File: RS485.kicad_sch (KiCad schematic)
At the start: 18 parts, among them CN4 WJ15EDGRC-3.81-2P, Q3 CJ3134K, U11 CA-IS3721HS, U12 π131U30, U13 SIT3485ESA, U14 ISO3082DWR

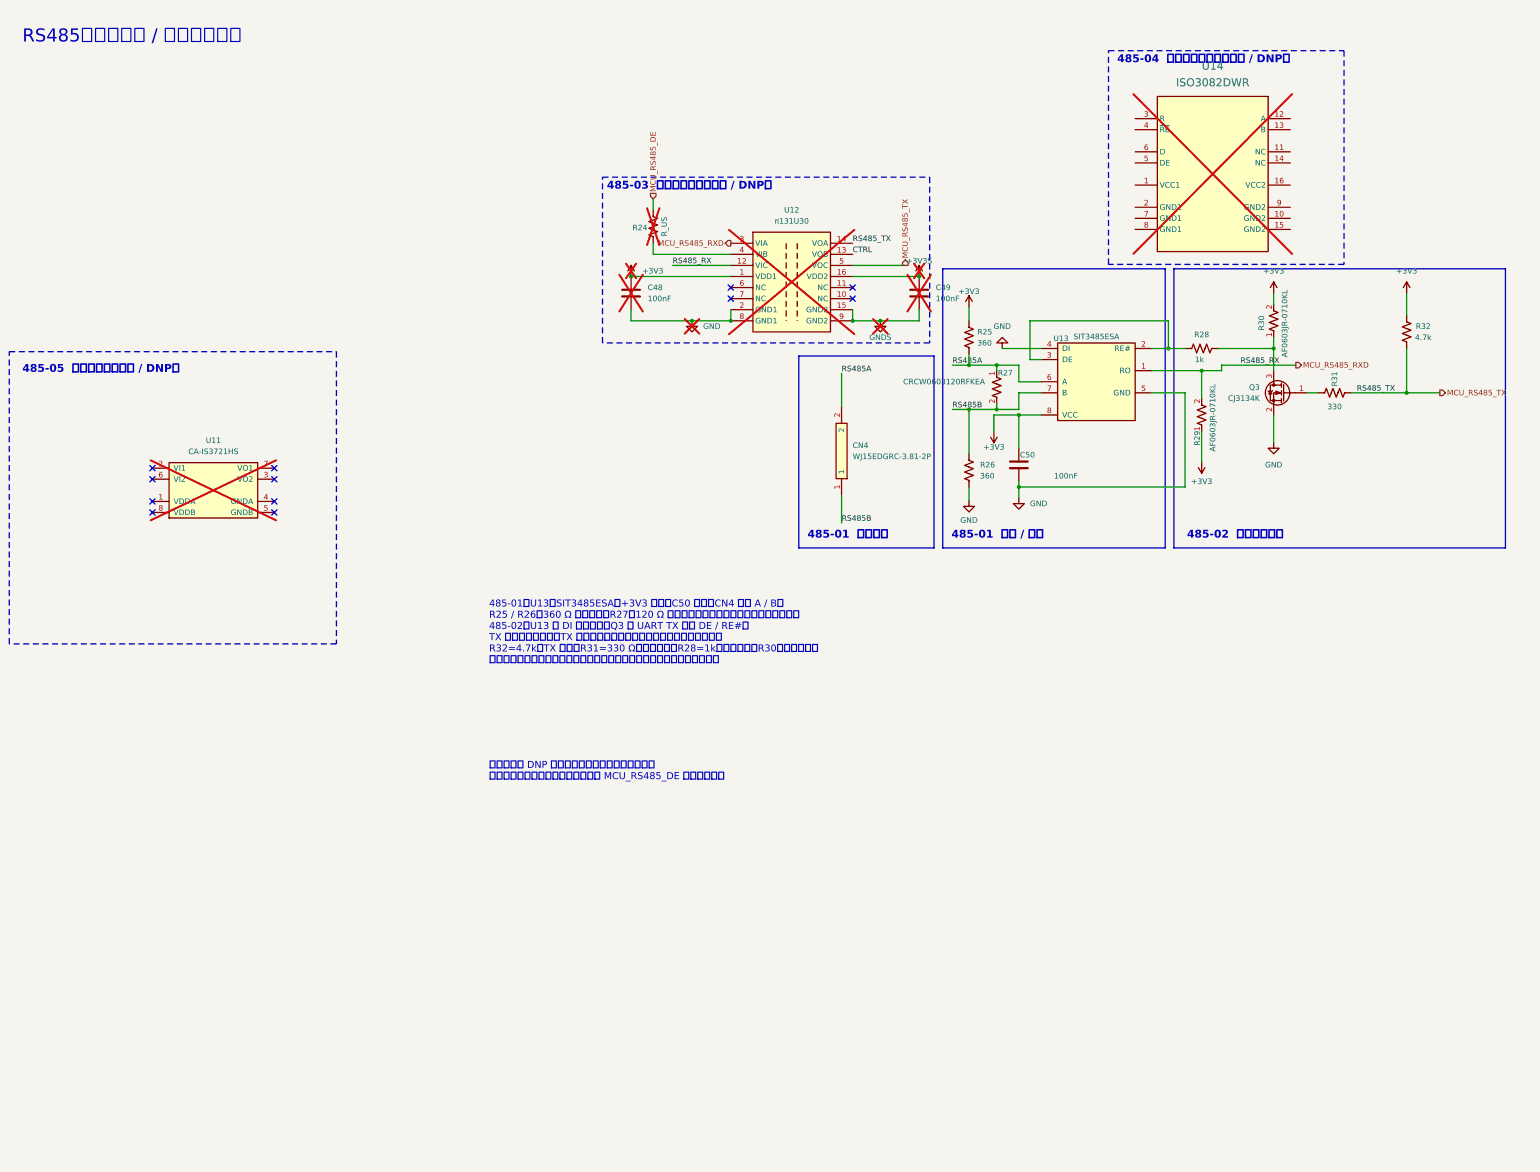
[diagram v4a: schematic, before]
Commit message: 更新V2.0电路设计及0.5oz内层制造交付资料
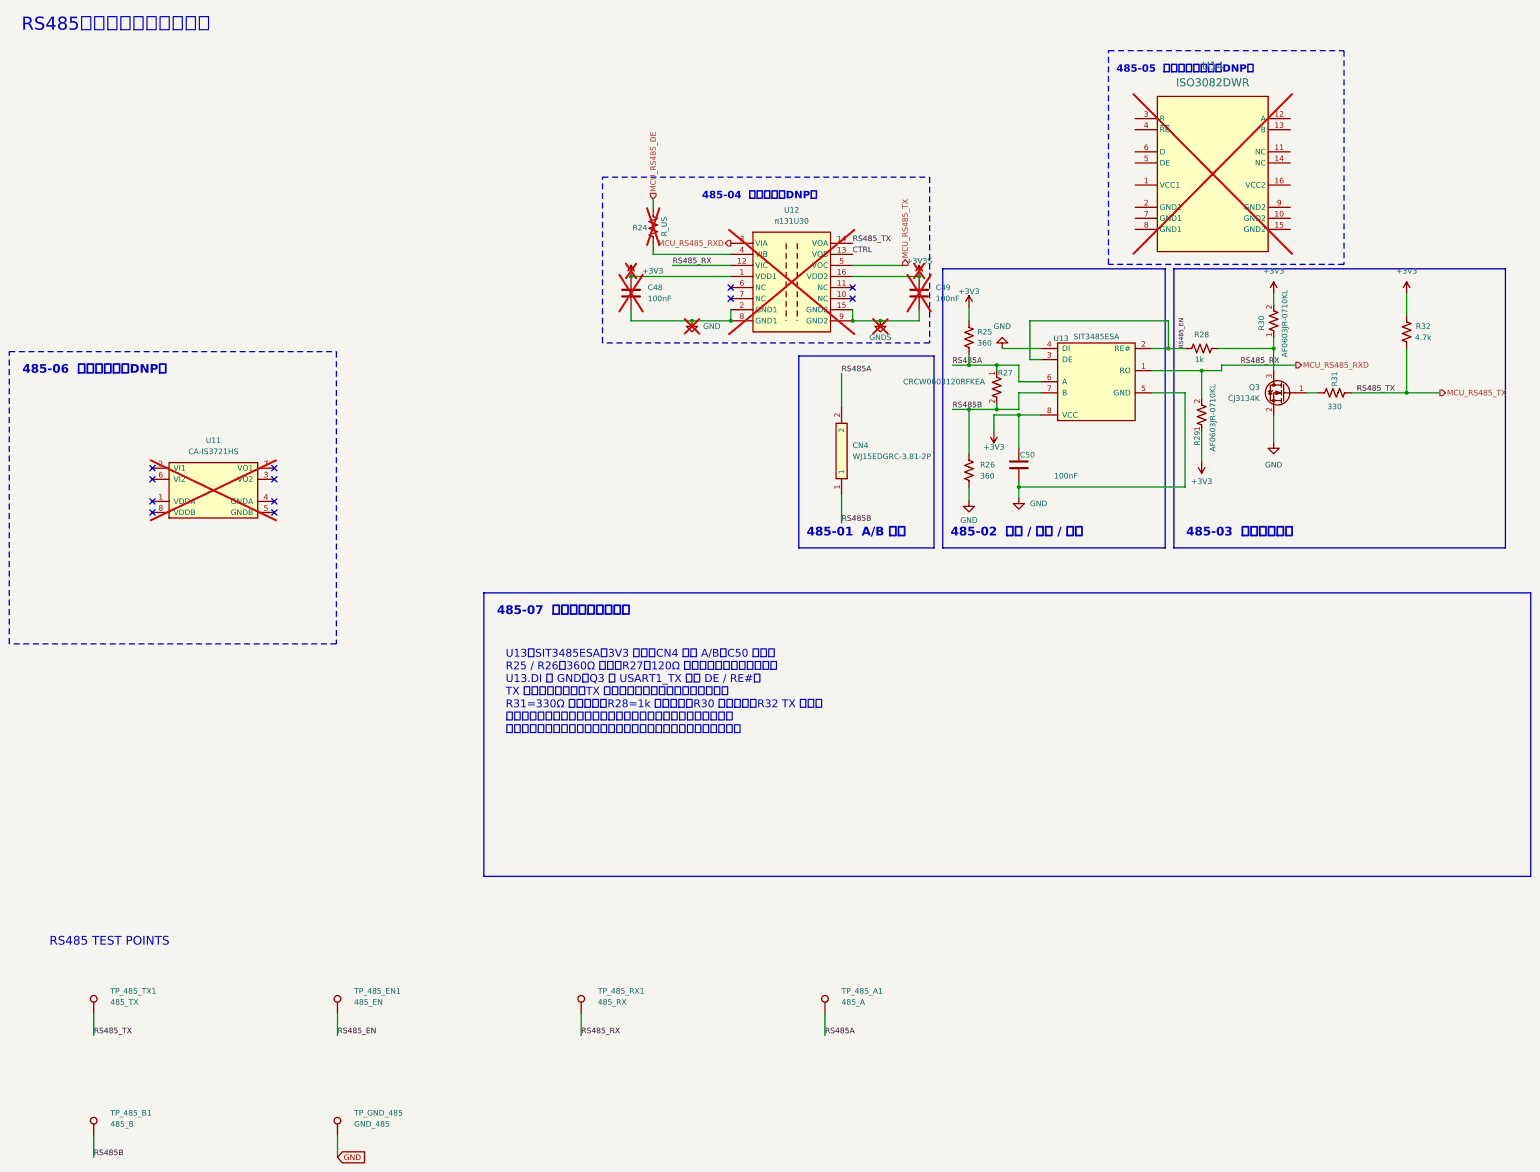
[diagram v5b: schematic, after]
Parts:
- added TP_485_A1: 485_A, kicad_api_lib:TestPoint_Pad_D0.762mm, symbol Connector:TestPoint
- added TP_485_B1: 485_B, kicad_api_lib:TestPoint_Pad_D0.762mm, symbol Connector:TestPoint
- added TP_485_EN1: 485_EN, kicad_api_lib:TestPoint_Pad_D0.762mm, symbol Connector:TestPoint
- added TP_485_RX1: 485_RX, kicad_api_lib:TestPoint_Pad_D0.762mm, symbol Connector:TestPoint
- added TP_485_TX1: 485_TX, kicad_api_lib:TestPoint_Pad_D0.762mm, symbol Connector:TestPoint
- added TP_GND_485: GND_485, kicad_api_lib:TestPoint_Pad_D1.016mm, symbol Connector:TestPoint
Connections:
- net GND: now also TP_GND_485.1
- net MCU_RS485_RXD: now also TP_485_RX1.1
- net MCU_RS485_TX: now also TP_485_TX1.1
- net RS485A: now also TP_485_A1.1
- net RS485B: now also TP_485_B1.1
- net RS485_EN: now reaches R28.1, U13.2 (RE#), U13.3 (DE)
- net RS485_EN: now also TP_485_EN1.1
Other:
- note added: "485-01 A/B 接口"
- note added: "485-02 收发 / 偏置 / 端接"
- note added: "485-03 自动收发方向"
- note added: "485-04 数字隔离【DNP】"
- note added: "485-05 隔离收发器预留【DNP】"
- note added: "485-06 隔离器备选【DNP】"
- note added: "485-07 工作原理与装配说明"
- note added: "RS485 TEST POINTS"
- note added: "RS485｜自动收发与备用隔离"
- note added: "U13：SIT3485ESA，3V3 供电；CN4 引出 A/B；C50 去耦。 R25 / R26：360Ω 偏置；R27：120Ω 端接，需按总线位置配置。 U13.DI 接 GND，Q3 由 USART1_TX 控制 DE / RE#。 TX 低：发送低电平；TX 高：释放总线，靠偏置恢复高电平。 R31=330Ω 栅极串阻；R28=1k 使能串阻；R30 使能上拉；R32 TX 上拉。 当前为共地方案；备用隔离电路不装配，不能据此认定整板隔离。 高电平恢复速度依赖偏置、端接及线缆电容，需按实际波特率验证。"
- note removed: "485-01 偏置 / 收发"
- note removed: "485-01 总线接口"
- note removed: "485-01｜U13：SIT3485ESA，+3V3 供电；C50 去耦；CN4 引出 A / B。 R25 / R26：360 Ω 总线偏置；R27：120 Ω 端接，需结合总线位置与另一端端接配置。 485-02｜U13 的 DI 固定接地；Q3 由 UART TX 控制 DE / RE#。 TX 低：发送低电平；TX 高：释放总线并接收，高电平由总线偏置恢复。 R32=4.7k：TX 上拉；R31=330 Ω：栅极串阻；R28=1k：使能串阻；R30：使能上拉。 该方式的高电平边沿受偏置、端接与线缆电容影响，应按实际波特率验证。"
- note removed: "485-02 自动方向控制"
- note removed: "485-03 数字隔离预留【备用 / DNP】"
- note removed: "485-04 隔离收发器预留【备用 / DNP】"
- note removed: "485-05 隔离器备选【备用 / DNP】"
- note removed: "RS485｜自动收发 / 备用隔离方案"
- note removed: "虚线分区为 DNP 备用器件，不构成当前工作链路。 当前使用共地的自动收发方案；独立 MCU_RS485_DE 为预留信号。"
